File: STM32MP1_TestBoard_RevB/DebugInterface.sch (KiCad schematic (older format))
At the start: 5 parts, among them SW2 SW_SPST, U1 STM32MP157xAB

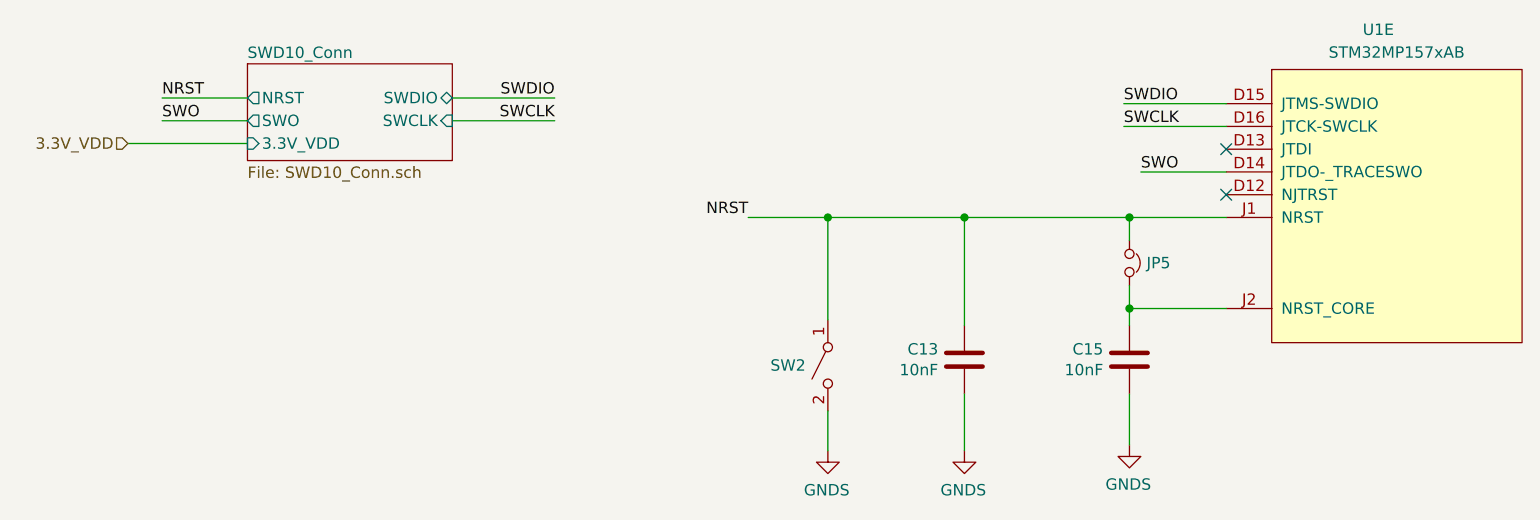
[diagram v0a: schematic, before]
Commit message: Updated design
- Added Crystal/Oscillators
- Replaced both SDMMC with single SDMMC w/ detect pin
- Added USB Type C for VIN
- Moved SWD pins
- Tidied up silk screen for pin headers J1, J2, J3, J4
- Moved DSI socket
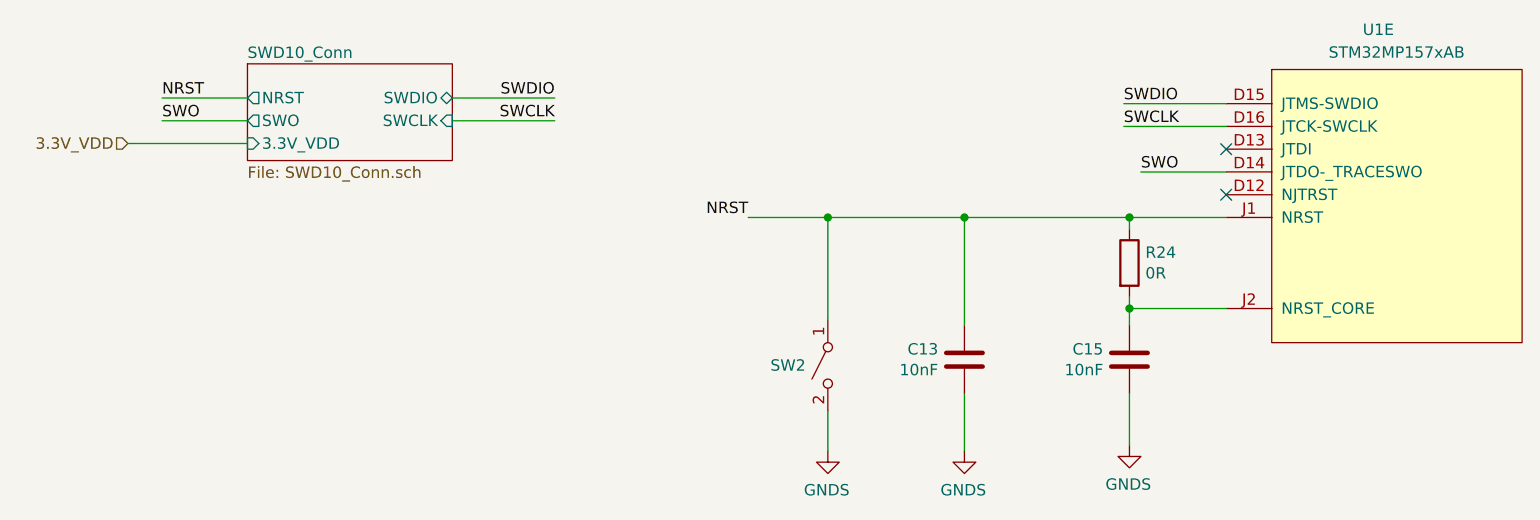
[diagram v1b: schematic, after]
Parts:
- removed JP5: Jumper_NC_Small, Jumper:SolderJumper-2_P1.3mm_Bridged_RoundedPad1.0x1.5mm, symbol Device:Jumper_NC_Small
- added R24: 0R, Resistor_SMD:R_0402_1005Metric_Pad0.72x0.64mm_HandSolder, symbol Device:R
- C13, C15: LCSC (none) -> C15195
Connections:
- net NRST: now also R24.1
- net at C15.1, U1.J2 (NRST_CORE): now also R24.2
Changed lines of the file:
@@
 $Descr A3 16535 11693
 encoding utf-8
-Sheet 4 10
+Sheet 4 9
 Title ""
 Date ""
@@
 F 4 "~" H 7750 6500 50  0001 C CNN "Mfr"
 F 5 "~" H 7750 6500 50  0001 C CNN "PartNo"
+F 6 "~" H 7750 6500 50  0001 C CNN "LCSC"
 	1    7750 6500
 	0    -1   1    0
@@
 F 4 "~" H 8350 6475 50  0001 C CNN "Mfr"
 F 5 "~" H 8350 6475 50  0001 C CNN "PartNo"
+F 6 "C15195" H 8350 6475 50  0001 C CNN "LCSC"
 	1    8350 6475
 	-1   0    0    -1
@@
 F 4 "~" H 9075 6475 50  0001 C CNN "Mfr"
 F 5 "~" H 9075 6475 50  0001 C CNN "PartNo"
+F 6 "C15195" H 9075 6475 50  0001 C CNN "LCSC"
 	1    9075 6475
 	-1   0    0    -1
 $EndComp
 Wire Wire Line
-	8350 5850 9075 5850
-$Comp
-L Device:Jumper_NC_Small JP5
-U 1 1 607CA98E
-P 9075 6050
-F 0 "JP5" V 9075 6125 50  0000 L CNN
-F 1 "Jumper_NC_Small" V 9120 6124 50  0001 L CNN
-F 2 "Jumper:SolderJumper-2_P1.3mm_Bridged_RoundedPad1.0x1.5mm" H 9075 6050 50  0001 C CNN
-F 3 "~" H 9075 6050 50  0001 C CNN
-F 4 "~" H 9075 6050 50  0001 C CNN "Mfr"
-F 5 "~" H 9075 6050 50  0001 C CNN "PartNo"
-	1    9075 6050
-	0    1    1    0
-$EndComp
-Wire Wire Line
-	9075 5950 9075 5850
-Connection ~ 9075 5850
-Wire Wire Line
-	9075 5850 9500 5850
-Wire Wire Line
-	9075 6150 9075 6250
-Wire Wire Line
 	9500 6250 9075 6250
-Connection ~ 9075 6250
 Wire Wire Line
 	9075 6250 9075 6325
@@
 F 4 "~" H 10250 5650 50  0001 C CNN "Mfr"
 F 5 "~" H 10250 5650 50  0001 C CNN "PartNo"
+F 6 "~" H 10250 5650 50  0001 C CNN "LCSC"
 	5    10250 5650
 	1    0    0    -1
 $EndComp
+$Comp
+L Device:R R24
+U 1 1 60917814
+P 9075 6050
+F 0 "R24" H 9145 6096 50  0000 L CNN
+F 1 "0R" H 9145 6005 50  0000 L CNN
+F 2 "Resistor_SMD:R_0402_1005Metric_Pad0.72x0.64mm_HandSolder" V 9005 6050 50  0001 C CNN
+F 3 "~" H 9075 6050 50  0001 C CNN
+	1    9075 6050
+	1    0    0    -1
+$EndComp
+Wire Wire Line
+	8350 5850 9075 5850
+Wire Wire Line
+	9075 6200 9075 6250
+Connection ~ 9075 6250
+Wire Wire Line
+	9075 5900 9075 5850
+Connection ~ 9075 5850
+Wire Wire Line
+	9075 5850 9500 5850
 $EndSCHEMATC

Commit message: completed revb layout
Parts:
- R24: LCSC (none) -> C25087
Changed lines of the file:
@@
 F 5 "~" H 7750 6500 50  0001 C CNN "PartNo"
 F 6 "~" H 7750 6500 50  0001 C CNN "LCSC"
+F 7 "~" H 7750 6500 50  0001 C CNN "Comment"
+F 8 "~" H 7750 6500 50  0001 C CNN "Mouser"
 	1    7750 6500
 	0    -1   1    0
@@
 F 5 "~" H 8350 6475 50  0001 C CNN "PartNo"
 F 6 "C15195" H 8350 6475 50  0001 C CNN "LCSC"
+F 7 "~" H 8350 6475 50  0001 C CNN "Comment"
+F 8 "~" H 8350 6475 50  0001 C CNN "Mouser"
 	1    8350 6475
 	-1   0    0    -1
@@
 F 5 "~" H 9075 6475 50  0001 C CNN "PartNo"
 F 6 "C15195" H 9075 6475 50  0001 C CNN "LCSC"
+F 7 "~" H 9075 6475 50  0001 C CNN "Comment"
+F 8 "~" H 9075 6475 50  0001 C CNN "Mouser"
 	1    9075 6475
 	-1   0    0    -1
@@
 F 5 "~" H 10250 5650 50  0001 C CNN "PartNo"
 F 6 "~" H 10250 5650 50  0001 C CNN "LCSC"
+F 7 "~" H 10250 5650 50  0001 C CNN "Comment"
+F 8 "~" H 10250 5650 50  0001 C CNN "Mouser"
 	5    10250 5650
 	1    0    0    -1
@@
 F 2 "Resistor_SMD:R_0402_1005Metric_Pad0.72x0.64mm_HandSolder" V 9005 6050 50  0001 C CNN
 F 3 "~" H 9075 6050 50  0001 C CNN
+F 4 "~" H 9075 6050 50  0001 C CNN "Comment"
+F 5 "~" H 9075 6050 50  0001 C CNN "Mouser"
+F 6 "C25087" H 9075 6050 50  0001 C CNN "LCSC"
 	1    9075 6050
 	1    0    0    -1
